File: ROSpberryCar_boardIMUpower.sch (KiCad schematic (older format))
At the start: 5 parts, among them P1 CONN_5, P2 CONN_5, P3 RASPI_CONN, P4 CONN_2, P5 CONN_5

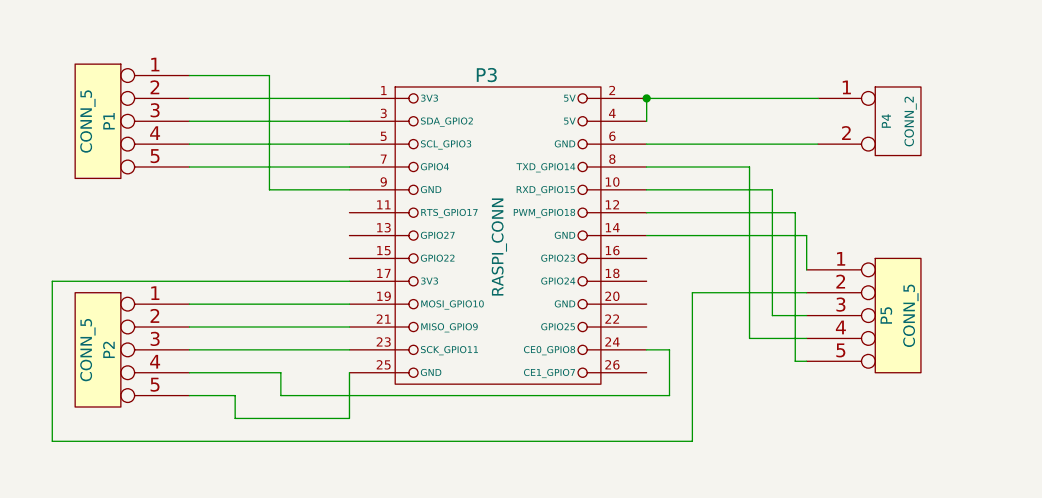
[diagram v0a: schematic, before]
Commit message: svg exported, added led
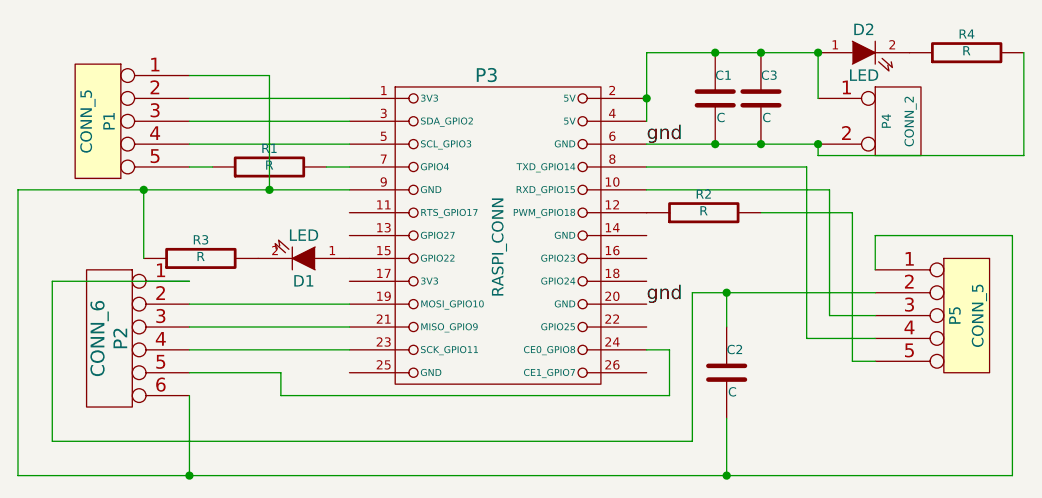
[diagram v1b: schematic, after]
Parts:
- removed P2: CONN_5, symbol CONN_5
- added C1, C2, C3: C, symbol C
- added D1, D2: LED, symbol LED
- added P2: CONN_6, symbol CONN_6
- added R1, R2, R3, R4: R, symbol R
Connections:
- net at P3.2 (5V), P3.4 (5V), P4.1 (P1): now also C1.1, C3.1, D2.1 (A)
- net gnd: now reaches P3.6 (GND), P4.2 (PM)
- net gnd: now also P3.20 (GND), C1.2, C3.2, R4.2
- net at P3.12 (PWM_GPIO18): now also R2.1; no longer P5.5
- net at P3.14 (GND): no longer P5.1
- net at P3.15 (GPIO22): now also D1.1 (A)
- net at P3.17 (3V3): no longer P5.2
- net at P3.19 (MOSI_GPIO10): now also P2.2
- net at P3.21 (MISO_GPIO9): now also P2.3
- net at P3.23 (SCK_GPIO11): now also P2.4
- net at P3.24 (CE0_GPIO8): now also P2.5
- net at P3.7 (GPIO4): now also R1.2; no longer P1.5
- net at P1.1, P3.9 (GND): now also P5.1, C2.2, P2.6, R3.1
- new net: P1.5, R1.1
- new net: C2.1, P2.1, P5.2
- new net: P5.5, R2.2
- new net: D2.2 (K), R4.1
- new net: D1.2 (K), R3.2
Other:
- moved on the sheet: P5
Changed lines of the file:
@@
 LIBS:raspi_conn
 LIBS:SparkFun
+LIBS:ROSpberryCar_boardIMUpower-cache
 EELAYER 24 0
 EELAYER END
@@
 L CONN_5 P5
 U 1 1 5293C5B2
-P 5850 3400
-F 0 "P5" V 5800 3400 50  0000 C CNN
-F 1 "CONN_5" V 5900 3400 50  0000 C CNN
-F 2 "" H 5850 3400 60  0000 C CNN
-F 3 "" H 5850 3400 60  0000 C CNN
-	1    5850 3400
-	1    0    0    -1
-$EndComp
-$Comp
-L CONN_5 P2
-U 1 1 5293C671
-P 2350 3550
-F 0 "P2" V 2300 3550 50  0000 C CNN
-F 1 "CONN_5" V 2400 3550 50  0000 C CNN
-F 2 "" H 2350 3550 60  0000 C CNN
-F 3 "" H 2350 3550 60  0000 C CNN
-	1    2350 3550
+P 6150 3400
+F 0 "P5" V 6100 3400 50  0000 C CNN
+F 1 "CONN_5" V 6200 3400 50  0000 C CNN
+F 2 "" H 6150 3400 60  0000 C CNN
+F 3 "" H 6150 3400 60  0000 C CNN
+	1    6150 3400
+	1    0    0    -1
+$EndComp
+Wire Wire Line
+	5500 2650 4750 2650
+Wire Wire Line
+	4750 2250 4750 2550
+Connection ~ 4750 2450
+Wire Wire Line
+	2750 2450 3450 2450
+Wire Wire Line
+	3450 2550 2750 2550
+Wire Wire Line
+	2750 2650 3450 2650
+Wire Wire Line
+	2000 2850 3450 2850
+Wire Wire Line
+	3100 2350 2750 2350
+Wire Wire Line
+	4950 3300 5750 3300
+Wire Wire Line
+	5750 3500 5450 3500
+Wire Wire Line
+	5450 3500 5450 2750
+Wire Wire Line
+	5450 2750 4750 2750
+Wire Wire Line
+	4750 2850 5550 2850
+Wire Wire Line
+	5550 2850 5550 3400
+Wire Wire Line
+	5550 3400 5750 3400
+Wire Wire Line
+	5650 2950 5650 3600
+Wire Wire Line
+	5650 3600 5750 3600
+Wire Wire Line
+	3100 2850 3100 2350
+Wire Wire Line
+	2750 3350 3450 3350
+Wire Wire Line
+	3450 3450 2750 3450
+Wire Wire Line
+	2750 3550 3450 3550
+Wire Wire Line
+	4750 3550 4850 3550
+Wire Wire Line
+	4850 3550 4850 3750
+Wire Wire Line
+	4850 3750 3150 3750
+Wire Wire Line
+	3150 3750 3150 3650
+Wire Wire Line
+	3150 3650 2750 3650
+Wire Wire Line
+	4950 3300 4950 3950
+Wire Wire Line
+	4950 3950 2150 3950
+Wire Wire Line
+	2150 3950 2150 3250
+$Comp
+L R R2
+U 1 1 52BC5DB6
+P 5000 2950
+F 0 "R2" V 5080 2950 40  0000 C CNN
+F 1 "R" V 5007 2951 40  0000 C CNN
+F 2 "" V 4930 2950 30  0000 C CNN
+F 3 "" H 5000 2950 30  0000 C CNN
+	1    5000 2950
+	0    -1   -1   0
+$EndComp
+Wire Wire Line
+	5250 2950 5650 2950
+$Comp
+L R R1
+U 1 1 52BC5E4A
+P 3100 2750
+F 0 "R1" V 3180 2750 40  0000 C CNN
+F 1 "R" V 3107 2751 40  0000 C CNN
+F 2 "" V 3030 2750 30  0000 C CNN
+F 3 "" H 3100 2750 30  0000 C CNN
+	1    3100 2750
+	0    -1   -1   0
+$EndComp
+Wire Wire Line
+	3350 2750 3450 2750
+Wire Wire Line
+	2750 2750 2850 2750
+$Comp
+L CONN_6 P2
+U 1 1 52BC68DE
+P 2400 3500
+F 0 "P2" V 2350 3500 60  0000 C CNN
+F 1 "CONN_6" V 2450 3500 60  0000 C CNN
+F 2 "" H 2400 3500 60  0000 C CNN
+F 3 "" H 2400 3500 60  0000 C CNN
+	1    2400 3500
 	-1   0    0    -1
 $EndComp
 Wire Wire Line
-	5500 2650 4750 2650
-Wire Wire Line
-	5500 2450 4750 2450
-Wire Wire Line
-	4750 2450 4750 2550
-Connection ~ 4750 2450
-Wire Wire Line
-	2750 2450 3450 2450
-Wire Wire Line
-	3450 2550 2750 2550
-Wire Wire Line
-	2750 2650 3450 2650
-Wire Wire Line
-	3450 2750 2750 2750
-Wire Wire Line
-	3450 2850 3100 2850
-Wire Wire Line
-	3100 2350 2750 2350
-Wire Wire Line
-	4950 3300 5450 3300
-Wire Wire Line
-	5450 3500 5200 3500
-Wire Wire Line
-	5200 3500 5200 2750
-Wire Wire Line
-	5200 2750 4750 2750
-Wire Wire Line
-	4750 2850 5300 2850
-Wire Wire Line
-	5300 2850 5300 3400
-Wire Wire Line
-	5300 3400 5450 3400
-Wire Wire Line
-	4750 2950 5400 2950
-Wire Wire Line
-	5400 2950 5400 3600
-Wire Wire Line
-	5400 3600 5450 3600
-Wire Wire Line
-	3100 2850 3100 2350
-Wire Wire Line
-	2750 3350 3450 3350
-Wire Wire Line
-	3450 3450 2750 3450
-Wire Wire Line
-	2750 3550 3450 3550
-Wire Wire Line
-	4750 3550 4850 3550
-Wire Wire Line
-	4850 3550 4850 3750
-Wire Wire Line
-	4850 3750 3150 3750
-Wire Wire Line
-	3150 3750 3150 3650
-Wire Wire Line
-	3150 3650 2750 3650
-Wire Wire Line
-	3450 3650 3450 3850
-Wire Wire Line
-	3450 3850 2950 3850
-Wire Wire Line
-	2950 3850 2950 3750
-Wire Wire Line
-	2950 3750 2750 3750
-Wire Wire Line
-	5450 3200 5450 3050
-Wire Wire Line
-	5450 3050 4750 3050
-Wire Wire Line
-	4950 3300 4950 3950
-Wire Wire Line
-	4950 3950 2150 3950
-Wire Wire Line
-	2150 3950 2150 3250
-Wire Wire Line
-	2150 3250 3450 3250
+	2150 3250 2750 3250
+Wire Wire Line
+	5750 3200 5750 3050
+Wire Wire Line
+	5750 3050 6350 3050
+Wire Wire Line
+	6350 3050 6350 4100
+Wire Wire Line
+	6350 4100 2000 4100
+Wire Wire Line
+	2000 4100 2000 2850
+Connection ~ 3100 2850
+$Comp
+L C C2
+U 1 1 52BC6AEC
+P 5100 3650
+F 0 "C2" H 5100 3750 40  0000 L CNN
+F 1 "C" H 5106 3565 40  0000 L CNN
+F 2 "" H 5138 3500 30  0000 C CNN
+F 3 "" H 5100 3650 60  0000 C CNN
+	1    5100 3650
+	1    0    0    -1
+$EndComp
+$Comp
+L C C1
+U 1 1 52BC6AF9
+P 5050 2450
+F 0 "C1" H 5050 2550 40  0000 L CNN
+F 1 "C" H 5056 2365 40  0000 L CNN
+F 2 "" H 5088 2300 30  0000 C CNN
+F 3 "" H 5050 2450 60  0000 C CNN
+	1    5050 2450
+	1    0    0    -1
+$EndComp
+$Comp
+L C C3
+U 1 1 52BC6AFF
+P 5250 2450
+F 0 "C3" H 5250 2550 40  0000 L CNN
+F 1 "C" H 5256 2365 40  0000 L CNN
+F 2 "" H 5288 2300 30  0000 C CNN
+F 3 "" H 5250 2450 60  0000 C CNN
+	1    5250 2450
+	1    0    0    -1
+$EndComp
+Wire Wire Line
+	4750 2250 5500 2250
+Wire Wire Line
+	5500 2250 5500 2450
+Connection ~ 5250 2250
+Connection ~ 5050 2250
+Wire Wire Line
+	5100 3450 5100 3300
+Connection ~ 5100 3300
+Wire Wire Line
+	5100 3850 5100 4100
+Connection ~ 5100 4100
+Connection ~ 5050 2650
+Connection ~ 5250 2650
+Text Label 4750 2650 0    60   ~ 0
+gnd
+Text Label 4750 3350 0    60   ~ 0
+gnd
+Wire Wire Line
+	2750 3750 2750 4100
+Connection ~ 2750 4100
+$Comp
+L LED D2
+U 1 1 52BC6F76
+P 5700 2250
+F 0 "D2" H 5700 2350 50  0000 C CNN
+F 1 "LED" H 5700 2150 50  0000 C CNN
+F 2 "" H 5700 2250 60  0000 C CNN
+F 3 "" H 5700 2250 60  0000 C CNN
+	1    5700 2250
+	1    0    0    -1
+$EndComp
+Connection ~ 5500 2250
+$Comp
+L R R4
+U 1 1 52BC6F87
+P 6150 2250
+F 0 "R4" V 6230 2250 40  0000 C CNN
+F 1 "R" V 6157 2251 40  0000 C CNN
+F 2 "" V 6080 2250 30  0000 C CNN
+F 3 "" H 6150 2250 30  0000 C CNN
+	1    6150 2250
+	0    -1   -1   0
+$EndComp
+Wire Wire Line
+	6400 2250 6400 2700
+Wire Wire Line
+	6400 2700 5500 2700
+Wire Wire Line
+	5500 2700 5500 2650
+Connection ~ 5500 2650
+$Comp
+L LED D1
+U 1 1 52BC6FC3
+P 3250 3150
+F 0 "D1" H 3250 3250 50  0000 C CNN
+F 1 "LED" H 3250 3050 50  0000 C CNN
+F 2 "" H 3250 3150 60  0000 C CNN
+F 3 "" H 3250 3150 60  0000 C CNN
+	1    3250 3150
+	-1   0    0    1
+$EndComp
+$Comp
+L R R3
+U 1 1 52BC6FC9
+P 2800 3150
+F 0 "R3" V 2880 3150 40  0000 C CNN
+F 1 "R" V 2807 3151 40  0000 C CNN
+F 2 "" V 2730 3150 30  0000 C CNN
+F 3 "" H 2800 3150 30  0000 C CNN
+	1    2800 3150
+	0    -1   -1   0
+$EndComp
+Wire Wire Line
+	2550 3150 2550 2850
+Connection ~ 2550 2850
 $EndSCHEMATC

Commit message: v2
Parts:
- removed P1, P5: CONN_5, symbol CONN_5
- removed R2, R3: R, symbol R
- added P1, P5: CONN_4, symbol CONN_4
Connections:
- net gnd: now also C2.2, P3.9 (GND), R1.1, P1.1 (P1), P5.1 (P1)
- net at P3.10 (RXD_GPIO15): now also P5.3 (P3)
- net at P3.13 (GPIO27): now also D1.1 (A)
- net at P3.15 (GPIO22): no longer D1.1 (A)
- net 3v3_2: now reaches P3.17 (3V3)
- net 3v3_2: now also P1.2 (P2)
- net at P3.25 (GND): now also P2.6
- net at P3.3 (SDA_GPIO2): now also P1.3 (P3)
- net at P3.5 (SCL_GPIO3): now also P1.4 (P4)
- net at P3.7 (GPIO4): no longer R1.2
- net at P3.8 (TXD_GPIO14): now also P5.4 (P4)
- net at C2.1, P2.1: now also P5.2 (P2)
- net at D1.2 (K): now also R1.2
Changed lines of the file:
@@
 $EndComp
-$Comp
-L CONN_5 P1
-U 1 1 5293C3D9
-P 2350 2550
-F 0 "P1" V 2300 2550 50  0000 C CNN
-F 1 "CONN_5" V 2400 2550 50  0000 C CNN
-F 2 "" H 2350 2550 60  0000 C CNN
-F 3 "" H 2350 2550 60  0000 C CNN
-	1    2350 2550
-	-1   0    0    -1
-$EndComp
-$Comp
-L CONN_5 P5
-U 1 1 5293C5B2
-P 6150 3400
-F 0 "P5" V 6100 3400 50  0000 C CNN
-F 1 "CONN_5" V 6200 3400 50  0000 C CNN
-F 2 "" H 6150 3400 60  0000 C CNN
-F 3 "" H 6150 3400 60  0000 C CNN
-	1    6150 3400
-	1    0    0    -1
-$EndComp
-Wire Wire Line
-	5500 2650 4750 2650
-Wire Wire Line
-	4750 2250 4750 2550
-Connection ~ 4750 2450
-Wire Wire Line
-	2750 2450 3450 2450
-Wire Wire Line
-	3450 2550 2750 2550
-Wire Wire Line
-	2750 2650 3450 2650
-Wire Wire Line
-	2000 2850 3450 2850
-Wire Wire Line
-	3100 2350 2750 2350
-Wire Wire Line
-	4950 3300 5750 3300
-Wire Wire Line
-	5750 3500 5450 3500
-Wire Wire Line
-	5450 3500 5450 2750
-Wire Wire Line
-	5450 2750 4750 2750
-Wire Wire Line
-	4750 2850 5550 2850
-Wire Wire Line
-	5550 2850 5550 3400
-Wire Wire Line
-	5550 3400 5750 3400
-Wire Wire Line
-	5650 2950 5650 3600
-Wire Wire Line
-	5650 3600 5750 3600
-Wire Wire Line
-	3100 2850 3100 2350
-Wire Wire Line
-	2750 3350 3450 3350
-Wire Wire Line
-	3450 3450 2750 3450
-Wire Wire Line
-	2750 3550 3450 3550
-Wire Wire Line
-	4750 3550 4850 3550
-Wire Wire Line
-	4850 3550 4850 3750
-Wire Wire Line
-	4850 3750 3150 3750
-Wire Wire Line
-	3150 3750 3150 3650
-Wire Wire Line
-	3150 3650 2750 3650
-Wire Wire Line
-	4950 3300 4950 3950
-Wire Wire Line
-	4950 3950 2150 3950
-Wire Wire Line
-	2150 3950 2150 3250
-$Comp
-L R R2
-U 1 1 52BC5DB6
-P 5000 2950
-F 0 "R2" V 5080 2950 40  0000 C CNN
-F 1 "R" V 5007 2951 40  0000 C CNN
-F 2 "" V 4930 2950 30  0000 C CNN
-F 3 "" H 5000 2950 30  0000 C CNN
-	1    5000 2950
-	0    -1   -1   0
-$EndComp
-Wire Wire Line
-	5250 2950 5650 2950
-$Comp
-L R R1
-U 1 1 52BC5E4A
-P 3100 2750
-F 0 "R1" V 3180 2750 40  0000 C CNN
-F 1 "R" V 3107 2751 40  0000 C CNN
-F 2 "" V 3030 2750 30  0000 C CNN
-F 3 "" H 3100 2750 30  0000 C CNN
-	1    3100 2750
-	0    -1   -1   0
-$EndComp
-Wire Wire Line
-	3350 2750 3450 2750
-Wire Wire Line
-	2750 2750 2850 2750
-$Comp
-L CONN_6 P2
-U 1 1 52BC68DE
-P 2400 3500
-F 0 "P2" V 2350 3500 60  0000 C CNN
-F 1 "CONN_6" V 2450 3500 60  0000 C CNN
-F 2 "" H 2400 3500 60  0000 C CNN
-F 3 "" H 2400 3500 60  0000 C CNN
-	1    2400 3500
-	-1   0    0    -1
-$EndComp
-Wire Wire Line
-	2150 3250 2750 3250
-Wire Wire Line
-	5750 3200 5750 3050
-Wire Wire Line
-	5750 3050 6350 3050
-Wire Wire Line
-	6350 3050 6350 4100
-Wire Wire Line
-	6350 4100 2000 4100
-Wire Wire Line
-	2000 4100 2000 2850
-Connection ~ 3100 2850
 $Comp
 L C C2
@@
 	1    0    0    -1
 $EndComp
-Wire Wire Line
-	4750 2250 5500 2250
-Wire Wire Line
-	5500 2250 5500 2450
-Connection ~ 5250 2250
-Connection ~ 5050 2250
-Wire Wire Line
-	5100 3450 5100 3300
-Connection ~ 5100 3300
-Wire Wire Line
-	5100 3850 5100 4100
-Connection ~ 5100 4100
-Connection ~ 5050 2650
-Connection ~ 5250 2650
 Text Label 4750 2650 0    60   ~ 0
 gnd
 Text Label 4750 3350 0    60   ~ 0
 gnd
-Wire Wire Line
-	2750 3750 2750 4100
-Connection ~ 2750 4100
 $Comp
 L LED D2
@@
 	1    0    0    -1
 $EndComp
-Connection ~ 5500 2250
 $Comp
 L R R4
@@
 $EndComp
 Wire Wire Line
+	5500 2650 4750 2650
+Wire Wire Line
+	4750 2250 4750 2550
+Connection ~ 4750 2450
+Wire Wire Line
+	3450 2550 2750 2550
+Wire Wire Line
+	2750 2650 3450 2650
+Wire Wire Line
+	2000 2850 3450 2850
+Wire Wire Line
+	4950 3300 5750 3300
+Wire Wire Line
+	5750 3500 5450 3500
+Wire Wire Line
+	5450 3500 5450 2750
+Wire Wire Line
+	5450 2750 4750 2750
+Wire Wire Line
+	4750 2850 5550 2850
+Wire Wire Line
+	5550 2850 5550 3400
+Wire Wire Line
+	5550 3400 5750 3400
+Wire Wire Line
+	2750 3350 3450 3350
+Wire Wire Line
+	3450 3450 2750 3450
+Wire Wire Line
+	2750 3550 3450 3550
+Wire Wire Line
+	4750 3550 4850 3550
+Wire Wire Line
+	4850 3550 4850 3750
+Wire Wire Line
+	4850 3750 3150 3750
+Wire Wire Line
+	3150 3750 3150 3650
+Wire Wire Line
+	3150 3650 2750 3650
+Wire Wire Line
+	4950 3300 4950 3950
+Wire Wire Line
+	4950 3950 2150 3950
+Wire Wire Line
+	2150 3950 2150 3250
+Wire Wire Line
+	2150 3250 2750 3250
+Wire Wire Line
+	5750 3200 5750 3050
+Wire Wire Line
+	5750 3050 6350 3050
+Wire Wire Line
+	6350 3050 6350 4100
+Wire Wire Line
+	6350 4100 2000 4100
+Wire Wire Line
+	2000 4100 2000 2850
+Wire Wire Line
+	4750 2250 5500 2250
+Wire Wire Line
+	5500 2250 5500 2450
+Connection ~ 5250 2250
+Connection ~ 5050 2250
+Wire Wire Line
+	5100 3450 5100 3300
+Connection ~ 5100 3300
+Wire Wire Line
+	5100 3850 5100 4100
+Connection ~ 5100 4100
+Connection ~ 5050 2650
+Connection ~ 5250 2650
+Connection ~ 5500 2250
+Wire Wire Line
 	6400 2250 6400 2700
 Wire Wire Line
@@
 	5500 2700 5500 2650
 Connection ~ 5500 2650
+Text Label 2750 2350 0    60   ~ 0
+gnd
+Text Label 3450 3250 2    60   ~ 0
+3v3_2
+Text Label 2750 2450 0    60   ~ 0
+3v3_2
+$Comp
+L CONN_4 P1
+U 1 1 52BE0C7F
+P 2400 2500
+F 0 "P1" V 2350 2500 50  0000 C CNN
+F 1 "CONN_4" V 2450 2500 50  0000 C CNN
+F 2 "" H 2400 2500 60  0000 C CNN
+F 3 "" H 2400 2500 60  0000 C CNN
+	1    2400 2500
+	-1   0    0    -1
+$EndComp
+$Comp
+L CONN_4 P5
+U 1 1 52BE0C95
+P 6100 3350
+F 0 "P5" V 6050 3350 50  0000 C CNN
+F 1 "CONN_4" V 6150 3350 50  0000 C CNN
+F 2 "" H 6100 3350 60  0000 C CNN
+F 3 "" H 6100 3350 60  0000 C CNN
+	1    6100 3350
+	1    0    0    -1
+$EndComp
+$Comp
+L CONN_6 P2
+U 1 1 52BE0CAF
+P 2400 3500
+F 0 "P2" V 2350 3500 60  0000 C CNN
+F 1 "CONN_6" V 2450 3500 60  0000 C CNN
+F 2 "" H 2400 3500 60  0000 C CNN
+F 3 "" H 2400 3500 60  0000 C CNN
+	1    2400 3500
+	-1   0    0    -1
+$EndComp
+Wire Wire Line
+	2750 3750 3050 3750
+Wire Wire Line
+	3050 3750 3050 3850
+Wire Wire Line
+	3050 3850 3450 3850
+Wire Wire Line
+	3450 3850 3450 3650
+Text Label 3250 2850 0    60   ~ 0
+gnd
 $Comp
 L LED D1
-U 1 1 52BC6FC3
-P 3250 3150
-F 0 "D1" H 3250 3250 50  0000 C CNN
-F 1 "LED" H 3250 3050 50  0000 C CNN
-F 2 "" H 3250 3150 60  0000 C CNN
-F 3 "" H 3250 3150 60  0000 C CNN
-	1    3250 3150
+U 1 1 52BE1349
+P 3250 3050
+F 0 "D1" H 3250 3150 50  0000 C CNN
+F 1 "LED" H 3250 2950 50  0000 C CNN
+F 2 "" H 3250 3050 60  0000 C CNN
+F 3 "" H 3250 3050 60  0000 C CNN
+	1    3250 3050
 	-1   0    0    1
 $EndComp
 $Comp
-L R R3
-U 1 1 52BC6FC9
-P 2800 3150
-F 0 "R3" V 2880 3150 40  0000 C CNN
-F 1 "R" V 2807 3151 40  0000 C CNN
-F 2 "" V 2730 3150 30  0000 C CNN
-F 3 "" H 2800 3150 30  0000 C CNN
-	1    2800 3150
+L R R1
+U 1 1 52BE134F
+P 2800 3050
+F 0 "R1" V 2880 3050 40  0000 C CNN
+F 1 "R" V 2807 3051 40  0000 C CNN
+F 2 "" V 2730 3050 30  0000 C CNN
+F 3 "" H 2800 3050 30  0000 C CNN
+	1    2800 3050
 	0    -1   -1   0
 $EndComp
 Wire Wire Line
-	2550 3150 2550 2850
+	2550 3050 2550 2850
 Connection ~ 2550 2850
 $EndSCHEMATC
